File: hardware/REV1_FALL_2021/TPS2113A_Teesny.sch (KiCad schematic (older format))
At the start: 12 parts

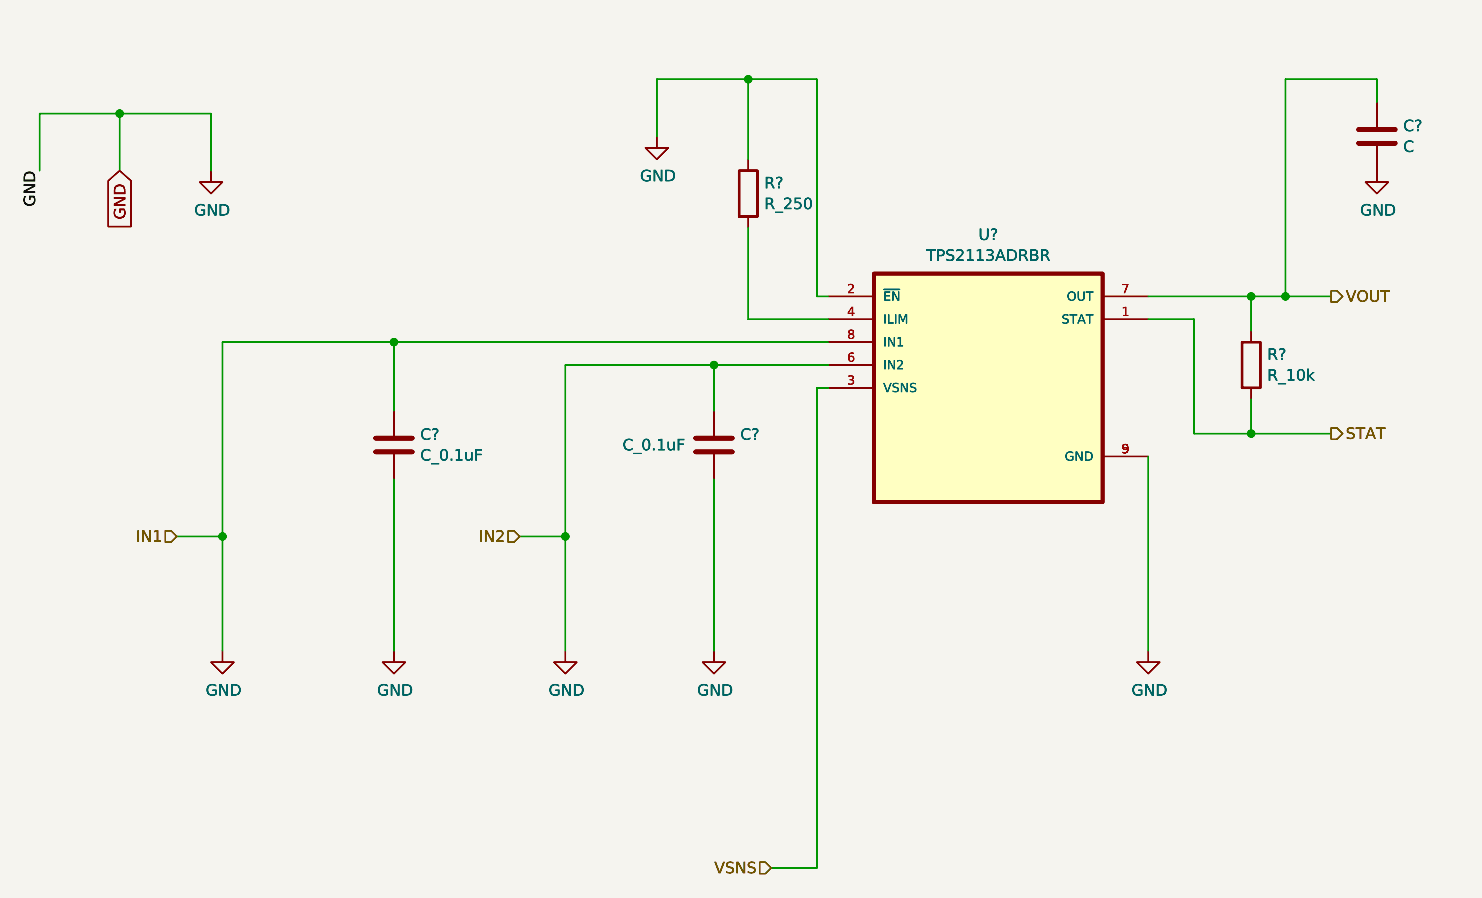
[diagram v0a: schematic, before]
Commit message: fix hierarchical sheet duplicates
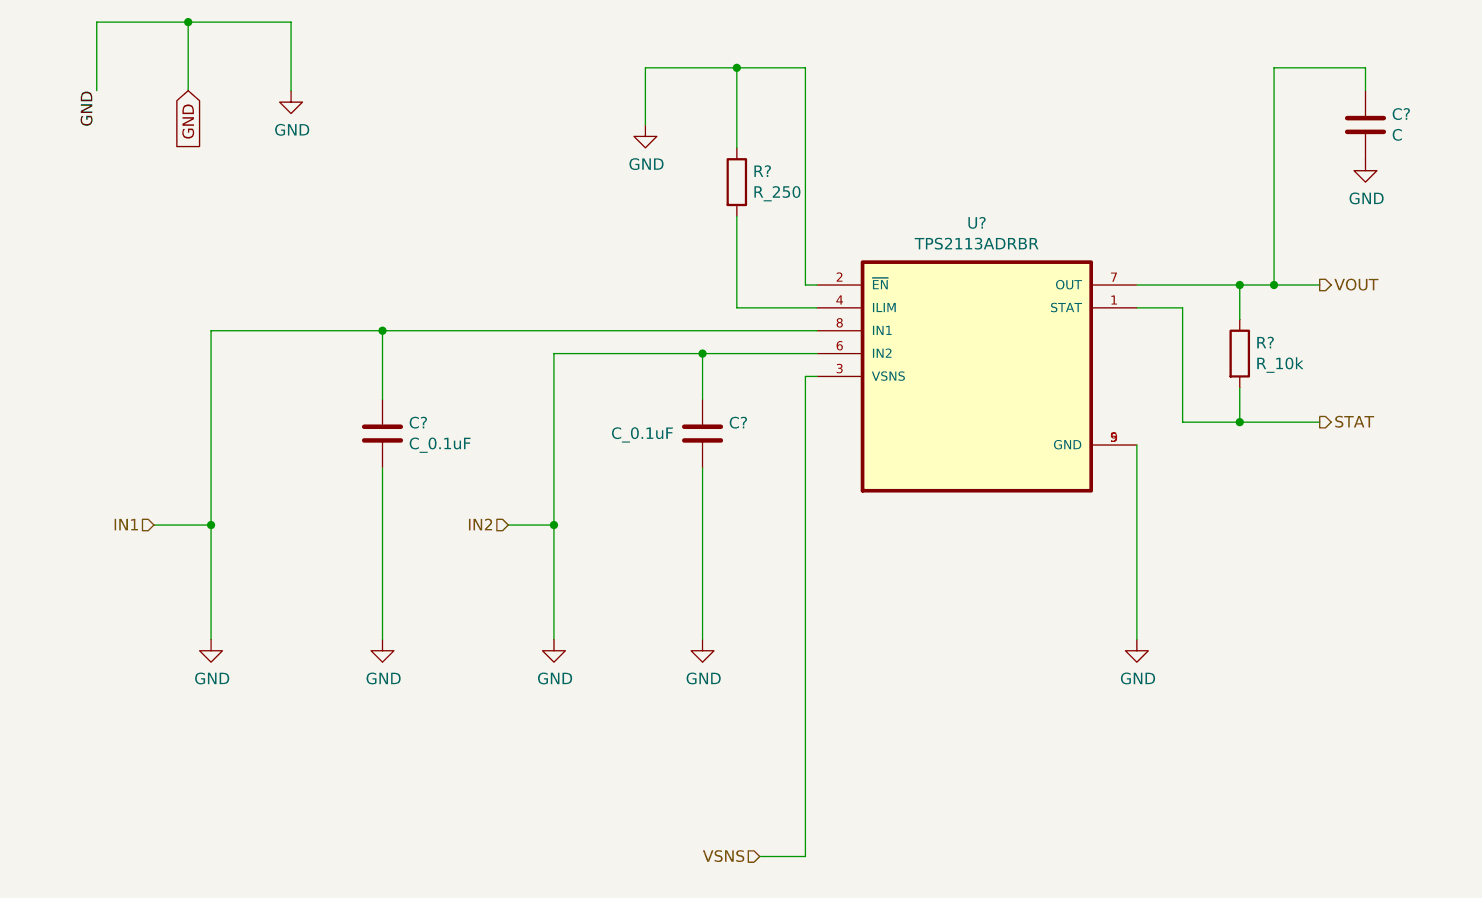
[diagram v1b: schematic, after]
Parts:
- removed C? (x4): C_0.1uF, symbol Device:C
- removed C? (x2): C, symbol Device:C
- removed R? (x2): R_250, symbol Device:R
- removed R? (x2): R_10k, symbol Device:R
- removed U? (x2): TPS2113ADRBR, IC_DRV8601DRBT, symbol TPS2113ADRBR:TPS2113ADRBR
- added C? (x2): C_0.1uF, symbol Device:C
- added C?: C, symbol Device:C
- added R?: R_250, symbol Device:R
- added R?: R_10k, symbol Device:R
- added U?: TPS2113ADRBR, footprints:TPS2113ADRBR, symbol TPS2113ADRBR:TPS2113ADRBR
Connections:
- net GND: now also C?.1, C?.1, C?.2, C?.2, C?.2, R?.1, U?.2 (~EN), U?.5 (GND), U?.6 (IN2), U?.8 (IN1), U?.9 (GND)
- net STAT: now also R?.2, U?.1 (STAT)
- net VOUT: now also C?.1, R?.1, U?.7 (OUT)
- net VSNS: now also U?.3 (VSNS)
- new net: R?.2, U?.4 (ILIM)

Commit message: arrange and annotate schematic
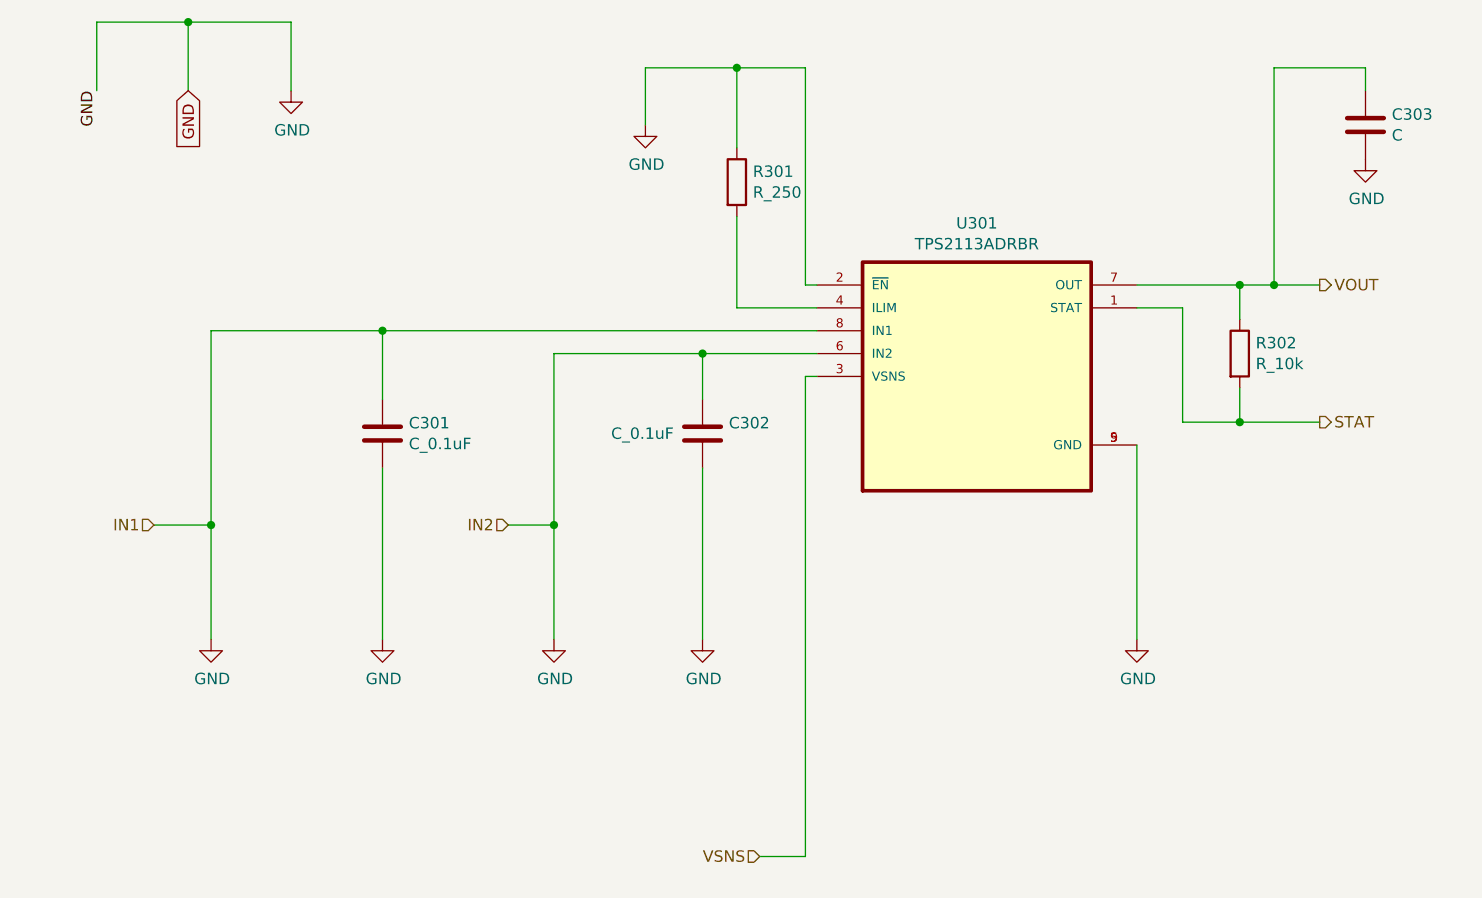
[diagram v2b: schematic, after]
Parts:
- gave numbers to parts that had none: 6
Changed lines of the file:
@@
 P 6600 3050
 AR Path="/61AB462E" Ref="U?"  Part="1"
-AR Path="/61A02CEE/61AB462E" Ref="U?"  Part="1"
-AR Path="/619AC3BC/61AB462E" Ref="U?"  Part="1"
-F 0 "U?" H 6600 3720 50  0000 C CNN
+AR Path="/61A02CEE/61AB462E" Ref="U201"  Part="1"
+AR Path="/619AC3BC/61AB462E" Ref="U301"  Part="1"
+F 0 "U301" H 6600 3720 50  0000 C CNN
 F 1 "TPS2113ADRBR" H 6600 3629 50  0000 C CNN
 F 2 "footprints:TPS2113ADRBR" H 6600 3050 50  0001 L BNN
@@
 P 4000 3300
 AR Path="/61AB4644" Ref="C?"  Part="1"
-AR Path="/619AC3BC/61AB4644" Ref="C?"  Part="1"
-AR Path="/61A02CEE/61AB4644" Ref="C?"  Part="1"
-F 0 "C?" H 4115 3346 50  0000 L CNN
+AR Path="/619AC3BC/61AB4644" Ref="C301"  Part="1"
+AR Path="/61A02CEE/61AB4644" Ref="C201"  Part="1"
+F 0 "C301" H 4115 3346 50  0000 L CNN
 F 1 "C_0.1uF" H 4115 3255 50  0000 L CNN
 F 2 "" H 4038 3150 50  0001 C CNN
@@
 P 5400 3300
 AR Path="/61AB464C" Ref="C?"  Part="1"
-AR Path="/619AC3BC/61AB464C" Ref="C?"  Part="1"
-AR Path="/61A02CEE/61AB464C" Ref="C?"  Part="1"
-F 0 "C?" H 5515 3346 50  0000 L CNN
+AR Path="/619AC3BC/61AB464C" Ref="C302"  Part="1"
+AR Path="/61A02CEE/61AB464C" Ref="C202"  Part="1"
+F 0 "C302" H 5515 3346 50  0000 L CNN
 F 1 "C_0.1uF" H 5000 3300 50  0000 L CNN
 F 2 "" H 5438 3150 50  0001 C CNN
@@
 P 5550 2200
 AR Path="/61AB465E" Ref="R?"  Part="1"
-AR Path="/619AC3BC/61AB465E" Ref="R?"  Part="1"
-AR Path="/61A02CEE/61AB465E" Ref="R?"  Part="1"
-F 0 "R?" H 5620 2246 50  0000 L CNN
+AR Path="/619AC3BC/61AB465E" Ref="R301"  Part="1"
+AR Path="/61A02CEE/61AB465E" Ref="R201"  Part="1"
+F 0 "R301" H 5620 2246 50  0000 L CNN
 F 1 "R_250" H 5620 2155 50  0000 L CNN
 F 2 "" V 5480 2200 50  0001 C CNN
@@
 P 5150 1950
 AR Path="/61AB4669" Ref="#PWR?"  Part="1"
-AR Path="/619AC3BC/61AB4669" Ref="#PWR?"  Part="1"
-AR Path="/61A02CEE/61AB4669" Ref="#PWR?"  Part="1"
-F 0 "#PWR?" H 5150 1700 50  0001 C CNN
+AR Path="/619AC3BC/61AB4669" Ref="#PWR0113"  Part="1"
+AR Path="/61A02CEE/61AB4669" Ref="#PWR0121"  Part="1"
+F 0 "#PWR0113" H 5150 1700 50  0001 C CNN
 F 1 "GND" H 5155 1777 50  0000 C CNN
 F 2 "" H 5150 1950 50  0001 C CNN
@@
 P 3250 4200
 AR Path="/61AB466F" Ref="#PWR?"  Part="1"
-AR Path="/619AC3BC/61AB466F" Ref="#PWR?"  Part="1"
-AR Path="/61A02CEE/61AB466F" Ref="#PWR?"  Part="1"
-F 0 "#PWR?" H 3250 3950 50  0001 C CNN
+AR Path="/619AC3BC/61AB466F" Ref="#PWR0114"  Part="1"
+AR Path="/61A02CEE/61AB466F" Ref="#PWR0122"  Part="1"
+F 0 "#PWR0114" H 3250 3950 50  0001 C CNN
 F 1 "GND" H 3255 4027 50  0000 C CNN
 F 2 "" H 3250 4200 50  0001 C CNN
@@
 P 4000 4200
 AR Path="/61AB4675" Ref="#PWR?"  Part="1"
-AR Path="/619AC3BC/61AB4675" Ref="#PWR?"  Part="1"
-AR Path="/61A02CEE/61AB4675" Ref="#PWR?"  Part="1"
-F 0 "#PWR?" H 4000 3950 50  0001 C CNN
+AR Path="/619AC3BC/61AB4675" Ref="#PWR0115"  Part="1"
+AR Path="/61A02CEE/61AB4675" Ref="#PWR0123"  Part="1"
+F 0 "#PWR0115" H 4000 3950 50  0001 C CNN
 F 1 "GND" H 4005 4027 50  0000 C CNN
 F 2 "" H 4000 4200 50  0001 C CNN
@@
 P 4750 4200
 AR Path="/61AB467B" Ref="#PWR?"  Part="1"
-AR Path="/619AC3BC/61AB467B" Ref="#PWR?"  Part="1"
-AR Path="/61A02CEE/61AB467B" Ref="#PWR?"  Part="1"
-F 0 "#PWR?" H 4750 3950 50  0001 C CNN
+AR Path="/619AC3BC/61AB467B" Ref="#PWR0116"  Part="1"
+AR Path="/61A02CEE/61AB467B" Ref="#PWR0124"  Part="1"
+F 0 "#PWR0116" H 4750 3950 50  0001 C CNN
 F 1 "GND" H 4755 4027 50  0000 C CNN
 F 2 "" H 4750 4200 50  0001 C CNN
@@
 P 5400 4200
 AR Path="/61AB4681" Ref="#PWR?"  Part="1"
-AR Path="/619AC3BC/61AB4681" Ref="#PWR?"  Part="1"
-AR Path="/61A02CEE/61AB4681" Ref="#PWR?"  Part="1"
-F 0 "#PWR?" H 5400 3950 50  0001 C CNN
+AR Path="/619AC3BC/61AB4681" Ref="#PWR0117"  Part="1"
+AR Path="/61A02CEE/61AB4681" Ref="#PWR0125"  Part="1"
+F 0 "#PWR0117" H 5400 3950 50  0001 C CNN
 F 1 "GND" H 5405 4027 50  0000 C CNN
 F 2 "" H 5400 4200 50  0001 C CNN
@@
 P 7300 4200
 AR Path="/61AB4687" Ref="#PWR?"  Part="1"
-AR Path="/619AC3BC/61AB4687" Ref="#PWR?"  Part="1"
-AR Path="/61A02CEE/61AB4687" Ref="#PWR?"  Part="1"
-F 0 "#PWR?" H 7300 3950 50  0001 C CNN
+AR Path="/619AC3BC/61AB4687" Ref="#PWR0118"  Part="1"
+AR Path="/61A02CEE/61AB4687" Ref="#PWR0126"  Part="1"
+F 0 "#PWR0118" H 7300 3950 50  0001 C CNN
 F 1 "GND" H 7305 4027 50  0000 C CNN
 F 2 "" H 7300 4200 50  0001 C CNN
@@
 P 7750 2950
 AR Path="/61AB46B4" Ref="R?"  Part="1"
-AR Path="/619AC3BC/61AB46B4" Ref="R?"  Part="1"
-AR Path="/61A02CEE/61AB46B4" Ref="R?"  Part="1"
-F 0 "R?" H 7820 2996 50  0000 L CNN
+AR Path="/619AC3BC/61AB46B4" Ref="R302"  Part="1"
+AR Path="/61A02CEE/61AB46B4" Ref="R202"  Part="1"
+F 0 "R302" H 7820 2996 50  0000 L CNN
 F 1 "R_10k" H 7820 2905 50  0000 L CNN
 F 2 "" V 7680 2950 50  0001 C CNN
@@
 P 8300 1950
 AR Path="/61AB46C3" Ref="C?"  Part="1"
-AR Path="/619AC3BC/61AB46C3" Ref="C?"  Part="1"
-AR Path="/61A02CEE/61AB46C3" Ref="C?"  Part="1"
-F 0 "C?" H 8415 1996 50  0000 L CNN
+AR Path="/619AC3BC/61AB46C3" Ref="C303"  Part="1"
+AR Path="/61A02CEE/61AB46C3" Ref="C203"  Part="1"
+F 0 "C303" H 8415 1996 50  0000 L CNN
 F 1 "C" H 8415 1905 50  0000 L CNN
 F 2 "" H 8338 1800 50  0001 C CNN
@@
 P 8300 2100
 AR Path="/61AB46CF" Ref="#PWR?"  Part="1"
-AR Path="/619AC3BC/61AB46CF" Ref="#PWR?"  Part="1"
-AR Path="/61A02CEE/61AB46CF" Ref="#PWR?"  Part="1"
-F 0 "#PWR?" H 8300 1850 50  0001 C CNN
+AR Path="/619AC3BC/61AB46CF" Ref="#PWR0119"  Part="1"
+AR Path="/61A02CEE/61AB46CF" Ref="#PWR0127"  Part="1"
+F 0 "#PWR0119" H 8300 1850 50  0001 C CNN
 F 1 "GND" H 8305 1927 50  0000 C CNN
 F 2 "" H 8300 2100 50  0001 C CNN
@@
 U 1 1 61ABB0D4
 P 3600 1800
-F 0 "#PWR?" H 3600 1550 50  0001 C CNN
+AR Path="/61ABB0D4" Ref="#PWR?"  Part="1"
+AR Path="/619AC3BC/61ABB0D4" Ref="#PWR0120"  Part="1"
+AR Path="/61A02CEE/61ABB0D4" Ref="#PWR0128"  Part="1"
+F 0 "#PWR0120" H 3600 1550 50  0001 C CNN
 F 1 "GND" H 3605 1627 50  0000 C CNN
 F 2 "" H 3600 1800 50  0001 C CNN

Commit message: assign footprints to all but battery holders
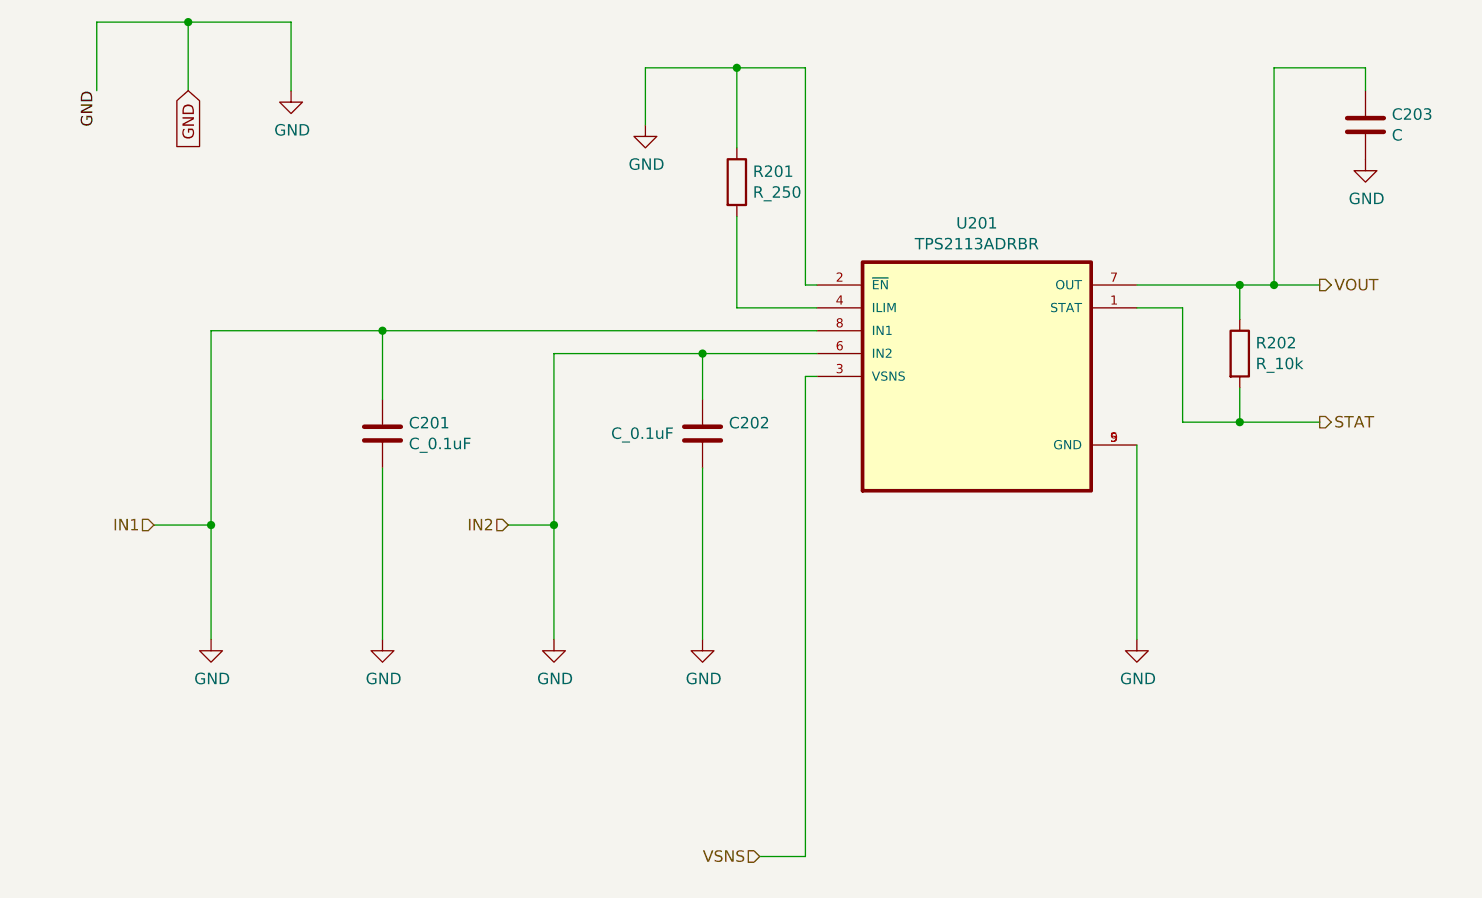
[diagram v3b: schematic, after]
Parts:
- C301, C302, C303: footprint (none) -> Capacitor_SMD:C_0805_2012Metric_Pad1.18x1.45mm_HandSolder
- R301, R302: footprint (none) -> Resistor_SMD:R_0805_2012Metric_Pad1.20x1.40mm_HandSolder
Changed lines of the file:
@@
 $Descr A4 11693 8268
 encoding utf-8
-Sheet 3 3
+Sheet 2 3
 Title ""
 Date ""
@@
 AR Path="/61A02CEE/61AB462E" Ref="U201"  Part="1"
 AR Path="/619AC3BC/61AB462E" Ref="U301"  Part="1"
-F 0 "U301" H 6600 3720 50  0000 C CNN
+F 0 "U201" H 6600 3720 50  0000 C CNN
 F 1 "TPS2113ADRBR" H 6600 3629 50  0000 C CNN
 F 2 "footprints:TPS2113ADRBR" H 6600 3050 50  0001 L BNN
@@
 AR Path="/619AC3BC/61AB4644" Ref="C301"  Part="1"
 AR Path="/61A02CEE/61AB4644" Ref="C201"  Part="1"
-F 0 "C301" H 4115 3346 50  0000 L CNN
+F 0 "C201" H 4115 3346 50  0000 L CNN
 F 1 "C_0.1uF" H 4115 3255 50  0000 L CNN
-F 2 "" H 4038 3150 50  0001 C CNN
+F 2 "Capacitor_SMD:C_0805_2012Metric_Pad1.18x1.45mm_HandSolder" H 4038 3150 50  0001 C CNN
 F 3 "~" H 4000 3300 50  0001 C CNN
 	1    4000 3300
@@
 AR Path="/619AC3BC/61AB464C" Ref="C302"  Part="1"
 AR Path="/61A02CEE/61AB464C" Ref="C202"  Part="1"
-F 0 "C302" H 5515 3346 50  0000 L CNN
+F 0 "C202" H 5515 3346 50  0000 L CNN
 F 1 "C_0.1uF" H 5000 3300 50  0000 L CNN
-F 2 "" H 5438 3150 50  0001 C CNN
+F 2 "Capacitor_SMD:C_0805_2012Metric_Pad1.18x1.45mm_HandSolder" H 5438 3150 50  0001 C CNN
 F 3 "~" H 5400 3300 50  0001 C CNN
 	1    5400 3300
@@
 AR Path="/619AC3BC/61AB465E" Ref="R301"  Part="1"
 AR Path="/61A02CEE/61AB465E" Ref="R201"  Part="1"
-F 0 "R301" H 5620 2246 50  0000 L CNN
+F 0 "R201" H 5620 2246 50  0000 L CNN
 F 1 "R_250" H 5620 2155 50  0000 L CNN
-F 2 "" V 5480 2200 50  0001 C CNN
+F 2 "Resistor_SMD:R_0805_2012Metric_Pad1.20x1.40mm_HandSolder" V 5480 2200 50  0001 C CNN
 F 3 "~" H 5550 2200 50  0001 C CNN
 	1    5550 2200
@@
 AR Path="/619AC3BC/61AB4669" Ref="#PWR0113"  Part="1"
 AR Path="/61A02CEE/61AB4669" Ref="#PWR0121"  Part="1"
-F 0 "#PWR0113" H 5150 1700 50  0001 C CNN
+F 0 "#PWR0121" H 5150 1700 50  0001 C CNN
 F 1 "GND" H 5155 1777 50  0000 C CNN
 F 2 "" H 5150 1950 50  0001 C CNN
@@
 AR Path="/619AC3BC/61AB466F" Ref="#PWR0114"  Part="1"
 AR Path="/61A02CEE/61AB466F" Ref="#PWR0122"  Part="1"
-F 0 "#PWR0114" H 3250 3950 50  0001 C CNN
+F 0 "#PWR0122" H 3250 3950 50  0001 C CNN
 F 1 "GND" H 3255 4027 50  0000 C CNN
 F 2 "" H 3250 4200 50  0001 C CNN
@@
 AR Path="/619AC3BC/61AB4675" Ref="#PWR0115"  Part="1"
 AR Path="/61A02CEE/61AB4675" Ref="#PWR0123"  Part="1"
-F 0 "#PWR0115" H 4000 3950 50  0001 C CNN
+F 0 "#PWR0123" H 4000 3950 50  0001 C CNN
 F 1 "GND" H 4005 4027 50  0000 C CNN
 F 2 "" H 4000 4200 50  0001 C CNN
@@
 AR Path="/619AC3BC/61AB467B" Ref="#PWR0116"  Part="1"
 AR Path="/61A02CEE/61AB467B" Ref="#PWR0124"  Part="1"
-F 0 "#PWR0116" H 4750 3950 50  0001 C CNN
+F 0 "#PWR0124" H 4750 3950 50  0001 C CNN
 F 1 "GND" H 4755 4027 50  0000 C CNN
 F 2 "" H 4750 4200 50  0001 C CNN
@@
 AR Path="/619AC3BC/61AB4681" Ref="#PWR0117"  Part="1"
 AR Path="/61A02CEE/61AB4681" Ref="#PWR0125"  Part="1"
-F 0 "#PWR0117" H 5400 3950 50  0001 C CNN
+F 0 "#PWR0125" H 5400 3950 50  0001 C CNN
 F 1 "GND" H 5405 4027 50  0000 C CNN
 F 2 "" H 5400 4200 50  0001 C CNN
@@
 AR Path="/619AC3BC/61AB4687" Ref="#PWR0118"  Part="1"
 AR Path="/61A02CEE/61AB4687" Ref="#PWR0126"  Part="1"
-F 0 "#PWR0118" H 7300 3950 50  0001 C CNN
+F 0 "#PWR0126" H 7300 3950 50  0001 C CNN
 F 1 "GND" H 7305 4027 50  0000 C CNN
 F 2 "" H 7300 4200 50  0001 C CNN
@@
 AR Path="/619AC3BC/61AB46B4" Ref="R302"  Part="1"
 AR Path="/61A02CEE/61AB46B4" Ref="R202"  Part="1"
-F 0 "R302" H 7820 2996 50  0000 L CNN
+F 0 "R202" H 7820 2996 50  0000 L CNN
 F 1 "R_10k" H 7820 2905 50  0000 L CNN
-F 2 "" V 7680 2950 50  0001 C CNN
+F 2 "Resistor_SMD:R_0805_2012Metric_Pad1.20x1.40mm_HandSolder" V 7680 2950 50  0001 C CNN
 F 3 "~" H 7750 2950 50  0001 C CNN
 	1    7750 2950
@@
 AR Path="/619AC3BC/61AB46C3" Ref="C303"  Part="1"
 AR Path="/61A02CEE/61AB46C3" Ref="C203"  Part="1"
-F 0 "C303" H 8415 1996 50  0000 L CNN
+F 0 "C203" H 8415 1996 50  0000 L CNN
 F 1 "C" H 8415 1905 50  0000 L CNN
-F 2 "" H 8338 1800 50  0001 C CNN
+F 2 "Capacitor_SMD:C_0805_2012Metric_Pad1.18x1.45mm_HandSolder" H 8338 1800 50  0001 C CNN
 F 3 "~" H 8300 1950 50  0001 C CNN
 	1    8300 1950
@@
 AR Path="/619AC3BC/61AB46CF" Ref="#PWR0119"  Part="1"
 AR Path="/61A02CEE/61AB46CF" Ref="#PWR0127"  Part="1"
-F 0 "#PWR0119" H 8300 1850 50  0001 C CNN
+F 0 "#PWR0127" H 8300 1850 50  0001 C CNN
 F 1 "GND" H 8305 1927 50  0000 C CNN
 F 2 "" H 8300 2100 50  0001 C CNN
@@
 AR Path="/619AC3BC/61ABB0D4" Ref="#PWR0120"  Part="1"
 AR Path="/61A02CEE/61ABB0D4" Ref="#PWR0128"  Part="1"
-F 0 "#PWR0120" H 3600 1550 50  0001 C CNN
+F 0 "#PWR0128" H 3600 1550 50  0001 C CNN
 F 1 "GND" H 3605 1627 50  0000 C CNN
 F 2 "" H 3600 1800 50  0001 C CNN
